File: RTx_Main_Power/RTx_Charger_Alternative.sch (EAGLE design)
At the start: 11 parts, among them IC1 TL331, Q1 STW11NM80

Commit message: Changes to RTx charger board.
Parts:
- removed U$3, U$4, U$5, U$7: TERMINAL, temp_library:TERMINAL_BATTERY
- removed U$6: 10, temp_library:TEH70
- added BT-, RELAY-, RELAY_A, VCC2: TERMINAL, temp_library:TERMINAL_BATTERY
- added R_CHARGE: 10, temp_library:TEH70
- renumbered U$2 to VCC1
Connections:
- net N$6 renamed REFERENCE
- removed net RELAY1: IC1.+IN, U$6.P$2, U$7.P$1
- removed net RELAY2: Q1.D(2), U$5.P$1
- new net RELAY-: Q1.D(2), RELAY-.P$1
- new net RELAY_A: IC1.+IN, RELAY_A.P$1, R_CHARGE.P$2
- net GND: now also BT-.P$1, R_CHARGE.P$3; no longer U$3.P$1, U$6.P$3
- net VCC2: now also R_CHARGE.P$1, VCC2.P$1; no longer U$4.P$1, U$6.P$1
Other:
- moved on the sheet: R1, R2
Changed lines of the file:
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@@
 <part name="Q1" library="temp_library" deviceset="STW11NM80" device="" value="STW11NM80"/>
 <part name="GND1" library="motorFeedback" deviceset="GND" device=""/>
-<part name="U$6" library="temp_library" deviceset="TEH70" device="" value="10"/>
-<part name="U$2" library="temp_library" deviceset="TERMINAL_BATTERY" device="" value="TERMINAL"/>
-<part name="U$3" library="temp_library" deviceset="TERMINAL_BATTERY" device="" value="TERMINAL"/>
-<part name="U$4" library="temp_library" deviceset="TERMINAL_BATTERY" device="" value="TERMINAL"/>
-<part name="U$5" library="temp_library" deviceset="TERMINAL_BATTERY" device="" value="TERMINAL"/>
-<part name="U$7" library="temp_library" deviceset="TERMINAL_BATTERY" device="" value="TERMINAL"/>
+<part name="R_CHARGE" library="temp_library" deviceset="TEH70" device="" value="10"/>
+<part name="VCC1" library="temp_library" deviceset="TERMINAL_BATTERY" device="" value="TERMINAL"/>
+<part name="BT-" library="temp_library" deviceset="TERMINAL_BATTERY" device="" value="TERMINAL"/>
+<part name="VCC2" library="temp_library" deviceset="TERMINAL_BATTERY" device="" value="TERMINAL"/>
+<part name="RELAY-" library="temp_library" deviceset="TERMINAL_BATTERY" device="" value="TERMINAL"/>
+<part name="RELAY_A" library="temp_library" deviceset="TERMINAL_BATTERY" device="" value="TERMINAL"/>
 <part name="R1" library="motorFeedback" deviceset="R-US_" device="R1206" value="10k"/>
 <part name="R2" library="motorFeedback" deviceset="R-US_" device="R1206" value="230k"/>
@@
 <instance part="R3" gate="G$1" x="200.66" y="91.44" rot="R180"/>
 <instance part="Q1" gate="G$1" x="210.82" y="99.06"/>
-<instance part="GND1" gate="1" x="134.62" y="53.34"/>
-<instance part="U$6" gate="G$1" x="154.94" y="93.98" rot="R90"/>
-<instance part="U$2" gate="G$1" x="109.22" y="88.9"/>
-<instance part="U$3" gate="G$1" x="109.22" y="66.04"/>
-<instance part="U$4" gate="G$1" x="109.22" y="106.68"/>
-<instance part="U$5" gate="G$1" x="218.44" y="121.92"/>
-<instance part="U$7" gate="G$1" x="172.72" y="121.92"/>
-<instance part="R1" gate="G$1" x="127" y="88.9" rot="R180"/>
-<instance part="R2" gate="G$1" x="142.24" y="76.2" rot="R270"/>
+<instance part="GND1" gate="1" x="134.62" y="66.04"/>
+<instance part="R_CHARGE" gate="G$1" x="154.94" y="99.06" rot="R90"/>
+<instance part="VCC1" gate="G$1" x="109.22" y="88.9"/>
+<instance part="BT-" gate="G$1" x="109.22" y="73.66"/>
+<instance part="VCC2" gate="G$1" x="109.22" y="104.14"/>
+<instance part="RELAY-" gate="G$1" x="218.44" y="116.84"/>
+<instance part="RELAY_A" gate="G$1" x="172.72" y="116.84"/>
+<instance part="R1" gate="G$1" x="132.08" y="88.9" rot="R180"/>
+<instance part="R2" gate="G$1" x="142.24" y="81.28" rot="R270"/>
 </instances>
 <busses>
@@
 <net name="VCC2" class="0">
 <segment>
-<wire x1="134.62" y1="93.98" x2="143.51" y2="93.98" width="0.1524" layer="91"/>
-<pinref part="U$6" gate="G$1" pin="P$1"/>
+<wire x1="134.62" y1="99.06" x2="143.51" y2="99.06" width="0.1524" layer="91"/>
+<pinref part="R_CHARGE" gate="G$1" pin="P$1"/>
 <pinref part="IC1" gate="G$1" pin="V+"/>
-<pinref part="U$4" gate="G$1" pin="P$1"/>
-<wire x1="185.42" y1="99.06" x2="185.42" y2="106.68" width="0.1524" layer="91"/>
-<wire x1="185.42" y1="106.68" x2="134.62" y2="106.68" width="0.1524" layer="91"/>
-<wire x1="134.62" y1="106.68" x2="109.22" y2="106.68" width="0.1524" layer="91"/>
-<wire x1="134.62" y1="93.98" x2="134.62" y2="106.68" width="0.1524" layer="91"/>
-<junction x="134.62" y="106.68"/>
-<label x="137.16" y="106.68" size="1.778" layer="95"/>
+<pinref part="VCC2" gate="G$1" pin="P$1"/>
+<wire x1="185.42" y1="99.06" x2="185.42" y2="104.14" width="0.1524" layer="91"/>
+<wire x1="185.42" y1="104.14" x2="134.62" y2="104.14" width="0.1524" layer="91"/>
+<wire x1="134.62" y1="104.14" x2="109.22" y2="104.14" width="0.1524" layer="91"/>
+<wire x1="134.62" y1="99.06" x2="134.62" y2="104.14" width="0.1524" layer="91"/>
+<junction x="134.62" y="104.14"/>
+<label x="137.16" y="104.14" size="1.778" layer="95"/>
 </segment>
 </net>
-<net name="RELAY1" class="0">
+<net name="RELAY_A" class="0">
 <segment>
-<wire x1="166.37" y1="93.98" x2="172.72" y2="93.98" width="0.1524" layer="91"/>
-<wire x1="172.72" y1="93.98" x2="172.72" y2="121.92" width="0.1524" layer="91"/>
-<pinref part="U$6" gate="G$1" pin="P$2"/>
-<pinref part="U$7" gate="G$1" pin="P$1"/>
-<label x="172.72" y="109.22" size="1.778" layer="95"/>
+<wire x1="166.37" y1="99.06" x2="172.72" y2="99.06" width="0.1524" layer="91"/>
+<wire x1="172.72" y1="99.06" x2="172.72" y2="116.84" width="0.1524" layer="91"/>
+<pinref part="R_CHARGE" gate="G$1" pin="P$2"/>
+<pinref part="RELAY_A" gate="G$1" pin="P$1"/>
+<label x="172.72" y="106.68" size="1.778" layer="95"/>
 <pinref part="IC1" gate="G$1" pin="+IN"/>
 <wire x1="177.8" y1="93.98" x2="172.72" y2="93.98" width="0.1524" layer="91"/>
-<junction x="172.72" y="93.98"/>
+<wire x1="172.72" y1="93.98" x2="172.72" y2="99.06" width="0.1524" layer="91"/>
+<junction x="172.72" y="99.06"/>
 </segment>
 </net>
-<net name="RELAY2" class="0">
+<net name="RELAY-" class="0">
 <segment>
 <pinref part="Q1" gate="G$1" pin="D(2)"/>
-<wire x1="218.44" y1="99.06" x2="218.44" y2="121.92" width="0.1524" layer="91"/>
-<pinref part="U$5" gate="G$1" pin="P$1"/>
-<label x="218.44" y="106.68" size="1.778" layer="95"/>
+<wire x1="218.44" y1="99.06" x2="218.44" y2="116.84" width="0.1524" layer="91"/>
+<pinref part="RELAY-" gate="G$1" pin="P$1"/>
+<label x="218.44" y="104.14" size="1.778" layer="95"/>
 </segment>
 </net>
-<net name="N$6" class="0">
+<net name="REFERENCE" class="0">
 <segment>
 <pinref part="IC1" gate="G$1" pin="-IN"/>
@@
 <pinref part="R1" gate="G$1" pin="1"/>
 <pinref part="R2" gate="G$1" pin="1"/>
-<wire x1="142.24" y1="88.9" x2="132.08" y2="88.9" width="0.1524" layer="91"/>
-<wire x1="142.24" y1="81.28" x2="142.24" y2="88.9" width="0.1524" layer="91"/>
+<wire x1="142.24" y1="88.9" x2="137.16" y2="88.9" width="0.1524" layer="91"/>
+<wire x1="142.24" y1="86.36" x2="142.24" y2="88.9" width="0.1524" layer="91"/>
 <junction x="142.24" y="88.9"/>
+<label x="162.56" y="88.9" size="1.778" layer="95"/>
 </segment>
 </net>
@@
 <segment>
 <pinref part="IC1" gate="G$1" pin="GND"/>
-<wire x1="185.42" y1="83.82" x2="185.42" y2="66.04" width="0.1524" layer="91"/>
-<wire x1="185.42" y1="66.04" x2="154.94" y2="66.04" width="0.1524" layer="91"/>
-<junction x="185.42" y="66.04"/>
-<wire x1="218.44" y1="66.04" x2="185.42" y2="66.04" width="0.1524" layer="91"/>
+<wire x1="185.42" y1="83.82" x2="185.42" y2="73.66" width="0.1524" layer="91"/>
+<wire x1="185.42" y1="73.66" x2="154.94" y2="73.66" width="0.1524" layer="91"/>
+<junction x="185.42" y="73.66"/>
+<wire x1="218.44" y1="73.66" x2="185.42" y2="73.66" width="0.1524" layer="91"/>
 <pinref part="Q1" gate="G$1" pin="S(3)"/>
-<wire x1="218.44" y1="83.82" x2="218.44" y2="66.04" width="0.1524" layer="91"/>
-<pinref part="U$6" gate="G$1" pin="P$3"/>
-<wire x1="154.94" y1="88.9" x2="154.94" y2="66.04" width="0.1524" layer="91"/>
-<junction x="154.94" y="66.04"/>
-<wire x1="154.94" y1="66.04" x2="142.24" y2="66.04" width="0.1524" layer="91"/>
+<wire x1="218.44" y1="83.82" x2="218.44" y2="73.66" width="0.1524" layer="91"/>
+<pinref part="R_CHARGE" gate="G$1" pin="P$3"/>
+<wire x1="154.94" y1="93.98" x2="154.94" y2="73.66" width="0.1524" layer="91"/>
+<junction x="154.94" y="73.66"/>
+<wire x1="154.94" y1="73.66" x2="142.24" y2="73.66" width="0.1524" layer="91"/>
 <pinref part="GND1" gate="1" pin="GND"/>
-<wire x1="142.24" y1="66.04" x2="134.62" y2="66.04" width="0.1524" layer="91"/>
-<wire x1="134.62" y1="55.88" x2="134.62" y2="66.04" width="0.1524" layer="91"/>
+<wire x1="142.24" y1="73.66" x2="134.62" y2="73.66" width="0.1524" layer="91"/>
+<wire x1="134.62" y1="68.58" x2="134.62" y2="73.66" width="0.1524" layer="91"/>
 <pinref part="R2" gate="G$1" pin="2"/>
-<wire x1="142.24" y1="66.04" x2="142.24" y2="71.12" width="0.1524" layer="91"/>
-<junction x="142.24" y="66.04"/>
-<pinref part="U$3" gate="G$1" pin="P$1"/>
-<wire x1="134.62" y1="66.04" x2="109.22" y2="66.04" width="0.1524" layer="91"/>
-<junction x="134.62" y="66.04"/>
+<wire x1="142.24" y1="73.66" x2="142.24" y2="76.2" width="0.1524" layer="91"/>
+<junction x="142.24" y="73.66"/>
+<pinref part="BT-" gate="G$1" pin="P$1"/>
+<wire x1="134.62" y1="73.66" x2="109.22" y2="73.66" width="0.1524" layer="91"/>
+<junction x="134.62" y="73.66"/>
 </segment>
 </net>
 <net name="VCC1" class="0">
 <segment>
-<pinref part="U$2" gate="G$1" pin="P$1"/>
+<pinref part="VCC1" gate="G$1" pin="P$1"/>
 <pinref part="R1" gate="G$1" pin="2"/>
-<wire x1="121.92" y1="88.9" x2="109.22" y2="88.9" width="0.1524" layer="91"/>
+<wire x1="127" y1="88.9" x2="109.22" y2="88.9" width="0.1524" layer="91"/>
 <label x="116.84" y="88.9" size="1.778" layer="95"/>
 </segment>

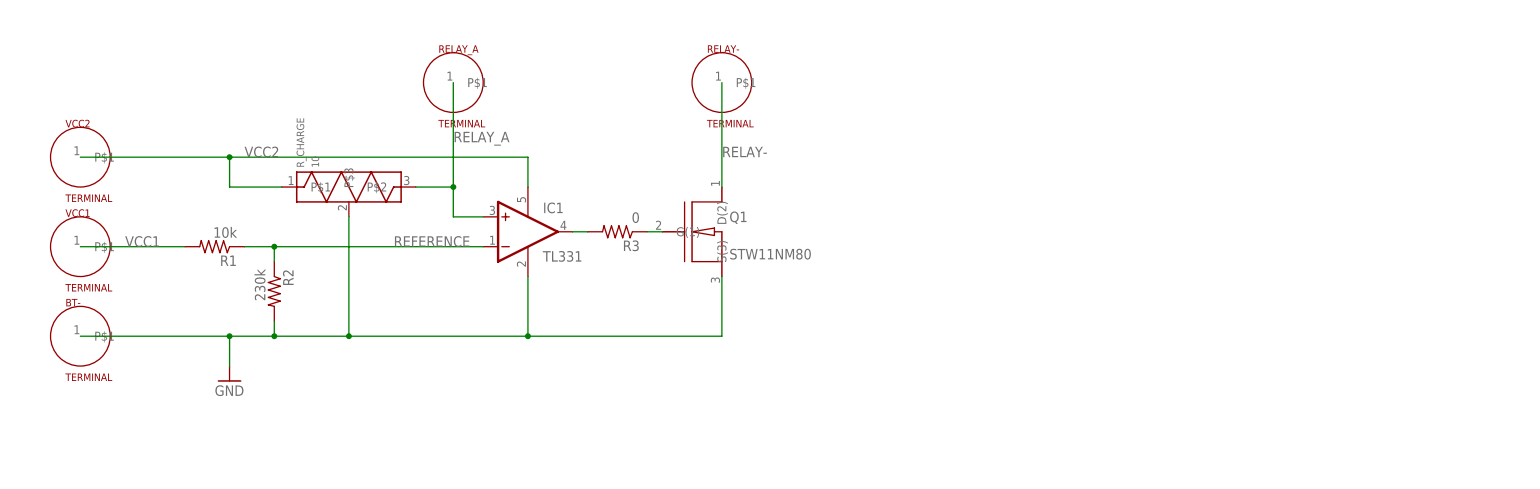
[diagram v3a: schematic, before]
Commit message: High speed signal routing information added to schematic. Updated Precharge board.
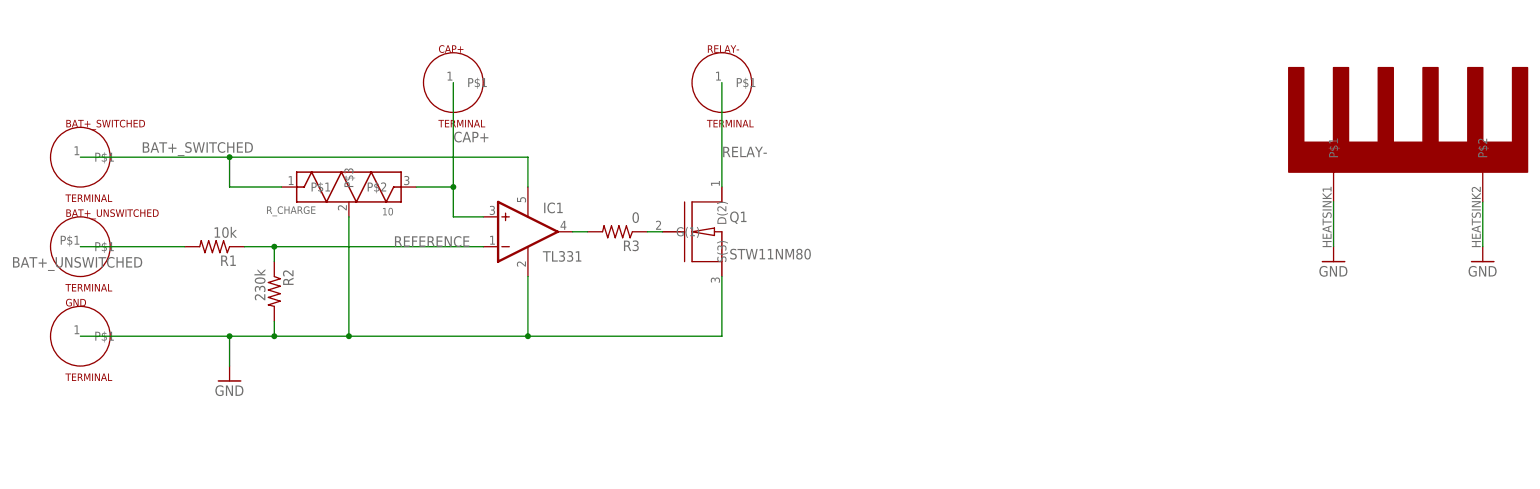
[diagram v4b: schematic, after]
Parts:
- removed VCC1: TERMINAL, temp_library:TERMINAL_BATTERY
- added BAT+_UNSWITCHED: TERMINAL, temp_library:TERMINAL_RELAY
- added HEATSINK: WA-T247-101E, temp_library:WA-T247-101E
- renumbered BT- to GND, RELAY_A to CAP+, VCC2 to BAT+_SWITCHED
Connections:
- net RELAY_A renamed CAP+
- net VCC2 renamed BAT+_SWITCHED
- removed net VCC1: R1.2, VCC1.P$1
- new net BAT+_UNSWITCHED: BAT+_UNSWITCHED.P$1, R1.2
- net GND: now also HEATSINK.P$1, HEATSINK.P$2
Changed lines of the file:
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@@
 <part name="GND1" library="motorFeedback" deviceset="GND" device=""/>
 <part name="R_CHARGE" library="temp_library" deviceset="TEH70" device="" value="10"/>
-<part name="VCC1" library="temp_library" deviceset="TERMINAL_BATTERY" device="" value="TERMINAL"/>
-<part name="BT-" library="temp_library" deviceset="TERMINAL_BATTERY" device="" value="TERMINAL"/>
-<part name="VCC2" library="temp_library" deviceset="TERMINAL_BATTERY" device="" value="TERMINAL"/>
+<part name="BAT+_UNSWITCHED" library="temp_library" deviceset="TERMINAL_RELAY" device="" value="TERMINAL"/>
+<part name="GND" library="temp_library" deviceset="TERMINAL_BATTERY" device="" value="TERMINAL"/>
+<part name="BAT+_SWITCHED" library="temp_library" deviceset="TERMINAL_BATTERY" device="" value="TERMINAL"/>
 <part name="RELAY-" library="temp_library" deviceset="TERMINAL_BATTERY" device="" value="TERMINAL"/>
-<part name="RELAY_A" library="temp_library" deviceset="TERMINAL_BATTERY" device="" value="TERMINAL"/>
+<part name="CAP+" library="temp_library" deviceset="TERMINAL_BATTERY" device="" value="TERMINAL"/>
 <part name="R1" library="motorFeedback" deviceset="R-US_" device="R1206" value="10k"/>
 <part name="R2" library="motorFeedback" deviceset="R-US_" device="R1206" value="230k"/>
+<part name="HEATSINK" library="temp_library" deviceset="WA-T247-101E" device=""/>
+<part name="GND2" library="motorFeedback" deviceset="GND" device=""/>
+<part name="GND3" library="motorFeedback" deviceset="GND" device=""/>
 </parts>
 <sheets>
@@
 <instance part="Q1" gate="G$1" x="210.82" y="99.06"/>
 <instance part="GND1" gate="1" x="134.62" y="66.04"/>
-<instance part="R_CHARGE" gate="G$1" x="154.94" y="99.06" rot="R90"/>
-<instance part="VCC1" gate="G$1" x="109.22" y="88.9"/>
-<instance part="BT-" gate="G$1" x="109.22" y="73.66"/>
-<instance part="VCC2" gate="G$1" x="109.22" y="104.14"/>
+<instance part="R_CHARGE" gate="G$1" x="154.94" y="99.06" smashed="yes" rot="R90">
+<attribute name="NAME" x="149.352" y="95.758" size="1.27" layer="95" rot="R180"/>
+<attribute name="VALUE" x="162.56" y="95.504" size="1.27" layer="96" rot="R180"/>
+</instance>
+<instance part="BAT+_UNSWITCHED" gate="G$1" x="109.22" y="88.9"/>
+<instance part="GND" gate="G$1" x="109.22" y="73.66"/>
+<instance part="BAT+_SWITCHED" gate="G$1" x="109.22" y="104.14"/>
 <instance part="RELAY-" gate="G$1" x="218.44" y="116.84"/>
-<instance part="RELAY_A" gate="G$1" x="172.72" y="116.84"/>
+<instance part="CAP+" gate="G$1" x="172.72" y="116.84"/>
 <instance part="R1" gate="G$1" x="132.08" y="88.9" rot="R180"/>
 <instance part="R2" gate="G$1" x="142.24" y="81.28" rot="R270"/>
+<instance part="HEATSINK" gate="G$1" x="335.28" y="104.14"/>
+<instance part="GND2" gate="1" x="322.58" y="86.36"/>
+<instance part="GND3" gate="1" x="347.98" y="86.36"/>
 </instances>
 <busses>
@@
 </segment>
 </net>
-<net name="VCC2" class="0">
+<net name="BAT+_SWITCHED" class="0">
 <segment>
 <wire x1="134.62" y1="99.06" x2="143.51" y2="99.06" width="0.1524" layer="91"/>
 <pinref part="R_CHARGE" gate="G$1" pin="P$1"/>
 <pinref part="IC1" gate="G$1" pin="V+"/>
-<pinref part="VCC2" gate="G$1" pin="P$1"/>
+<pinref part="BAT+_SWITCHED" gate="G$1" pin="P$1"/>
 <wire x1="185.42" y1="99.06" x2="185.42" y2="104.14" width="0.1524" layer="91"/>
 <wire x1="185.42" y1="104.14" x2="134.62" y2="104.14" width="0.1524" layer="91"/>
@@
 <wire x1="134.62" y1="99.06" x2="134.62" y2="104.14" width="0.1524" layer="91"/>
 <junction x="134.62" y="104.14"/>
-<label x="137.16" y="104.14" size="1.778" layer="95"/>
+<label x="119.634" y="104.902" size="1.778" layer="95"/>
 </segment>
 </net>
-<net name="RELAY_A" class="0">
+<net name="CAP+" class="0">
 <segment>
 <wire x1="166.37" y1="99.06" x2="172.72" y2="99.06" width="0.1524" layer="91"/>
 <wire x1="172.72" y1="99.06" x2="172.72" y2="116.84" width="0.1524" layer="91"/>
 <pinref part="R_CHARGE" gate="G$1" pin="P$2"/>
-<pinref part="RELAY_A" gate="G$1" pin="P$1"/>
+<pinref part="CAP+" gate="G$1" pin="P$1"/>
 <label x="172.72" y="106.68" size="1.778" layer="95"/>
 <pinref part="IC1" gate="G$1" pin="+IN"/>
@@
 <wire x1="142.24" y1="73.66" x2="142.24" y2="76.2" width="0.1524" layer="91"/>
 <junction x="142.24" y="73.66"/>
-<pinref part="BT-" gate="G$1" pin="P$1"/>
+<pinref part="GND" gate="G$1" pin="P$1"/>
 <wire x1="134.62" y1="73.66" x2="109.22" y2="73.66" width="0.1524" layer="91"/>
 <junction x="134.62" y="73.66"/>
 </segment>
+<segment>
+<pinref part="HEATSINK" gate="G$1" pin="P$1"/>
+<pinref part="GND2" gate="1" pin="GND"/>
+<wire x1="322.58" y1="88.9" x2="322.58" y2="96.52" width="0.1524" layer="91"/>
+</segment>
+<segment>
+<pinref part="HEATSINK" gate="G$1" pin="P$2"/>
+<pinref part="GND3" gate="1" pin="GND"/>
+<wire x1="347.98" y1="88.9" x2="347.98" y2="96.52" width="0.1524" layer="91"/>
+</segment>
 </net>
-<net name="VCC1" class="0">
+<net name="BAT+_UNSWITCHED" class="0">
 <segment>
-<pinref part="VCC1" gate="G$1" pin="P$1"/>
+<pinref part="BAT+_UNSWITCHED" gate="G$1" pin="P$1"/>
 <pinref part="R1" gate="G$1" pin="2"/>
 <wire x1="127" y1="88.9" x2="109.22" y2="88.9" width="0.1524" layer="91"/>
-<label x="116.84" y="88.9" size="1.778" layer="95"/>
+<label x="97.536" y="85.344" size="1.778" layer="95"/>
 </segment>
 </net>
